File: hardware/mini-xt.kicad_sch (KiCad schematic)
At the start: 0 parts

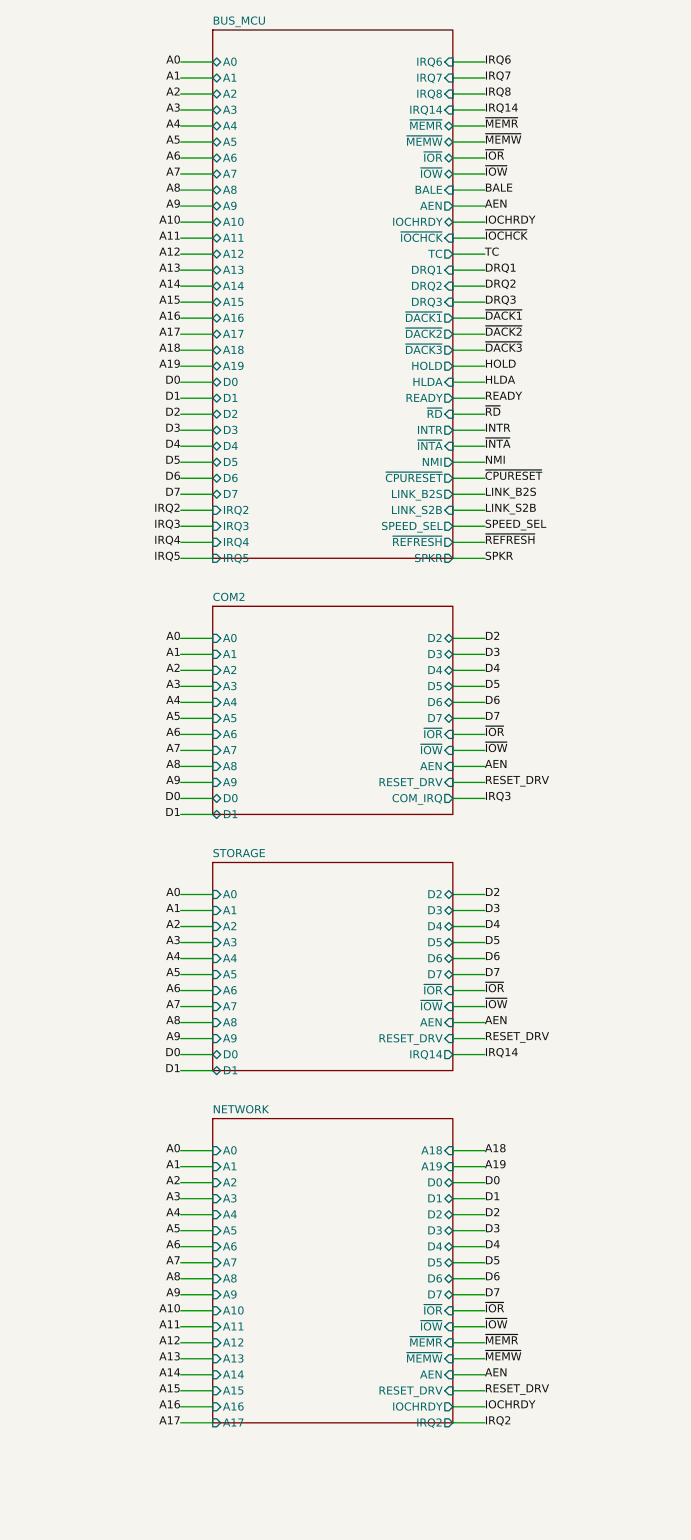
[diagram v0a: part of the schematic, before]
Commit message: bus_mcu: direct 3.3V bus GPIOs (LVC245s+DIR logic deleted); EXT IRQ/DRQ scan
Deleted all six 74LVC245A (data/strobes/address+BALE/AEN-TC) and their DIR
logic; each MCU GPIO now sits on its 3.3V bus net 1:1 (RP2350B is 5V-tolerant
and tri-states natively). Freed GPIO43 (ex-DATADIR) -> EXP_DDIR. Moved the
'165 IRQ collector, the counter '244 output-enable stage and its inverter to
+3V3 (74HC values). Added a 2x 74HC165 EXT scan chain (U19/U20) for the
expansion-port EXT_IRQ2-8/EXT_DRQ1-3 lines. Kept U14-U16 '244s (deviation
from the brief): they are the '163 counter's only tri-state, not level
shifters -- deleting them would fight cpu_core's '573 latches on A0-A19.

Co-Authored-By: Claude Fable 5 <noreply@anthropic.com>
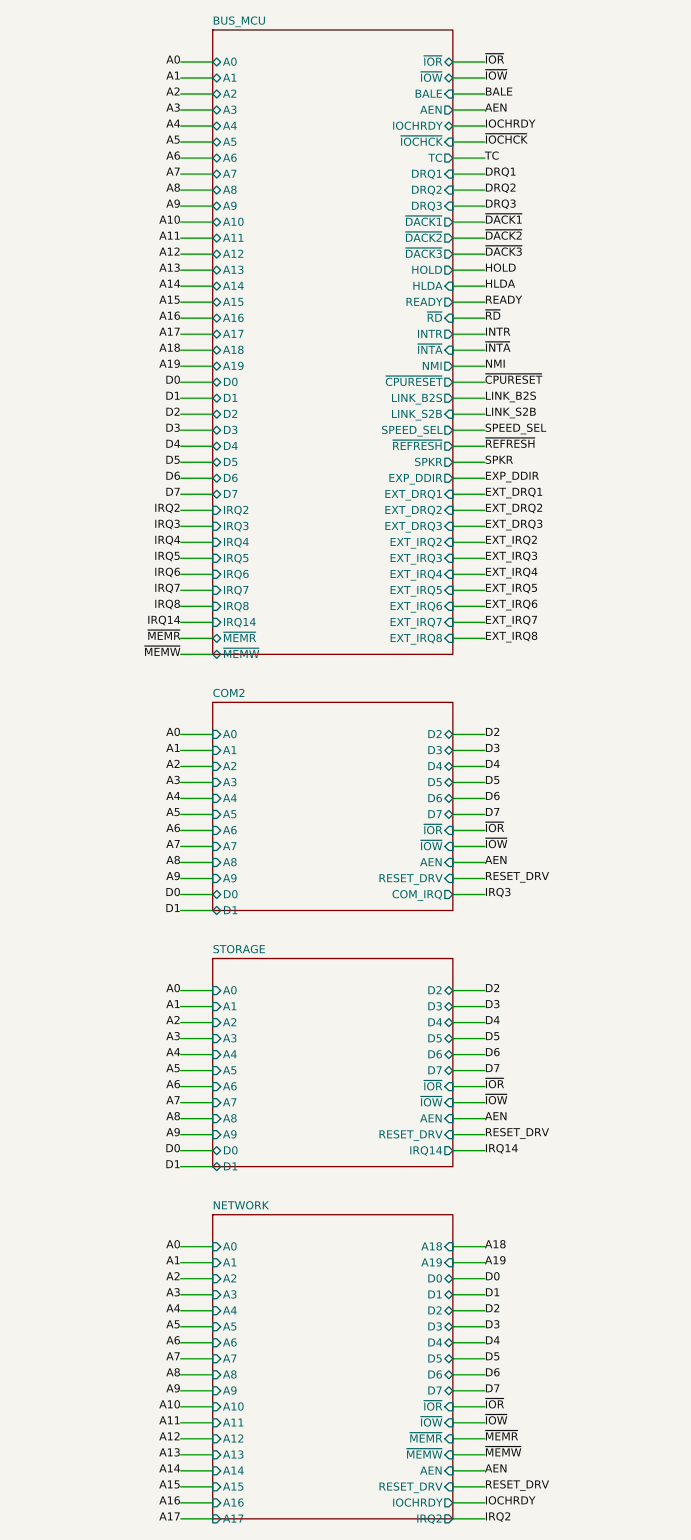
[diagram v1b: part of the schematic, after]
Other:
- sheet BUS_MCU ports: added EXP_DDIR, EXT_DRQ1, EXT_DRQ2, EXT_DRQ3, EXT_IRQ2, EXT_IRQ3, EXT_IRQ4, EXT_IRQ5, EXT_IRQ6, EXT_IRQ7, EXT_IRQ8; removed none

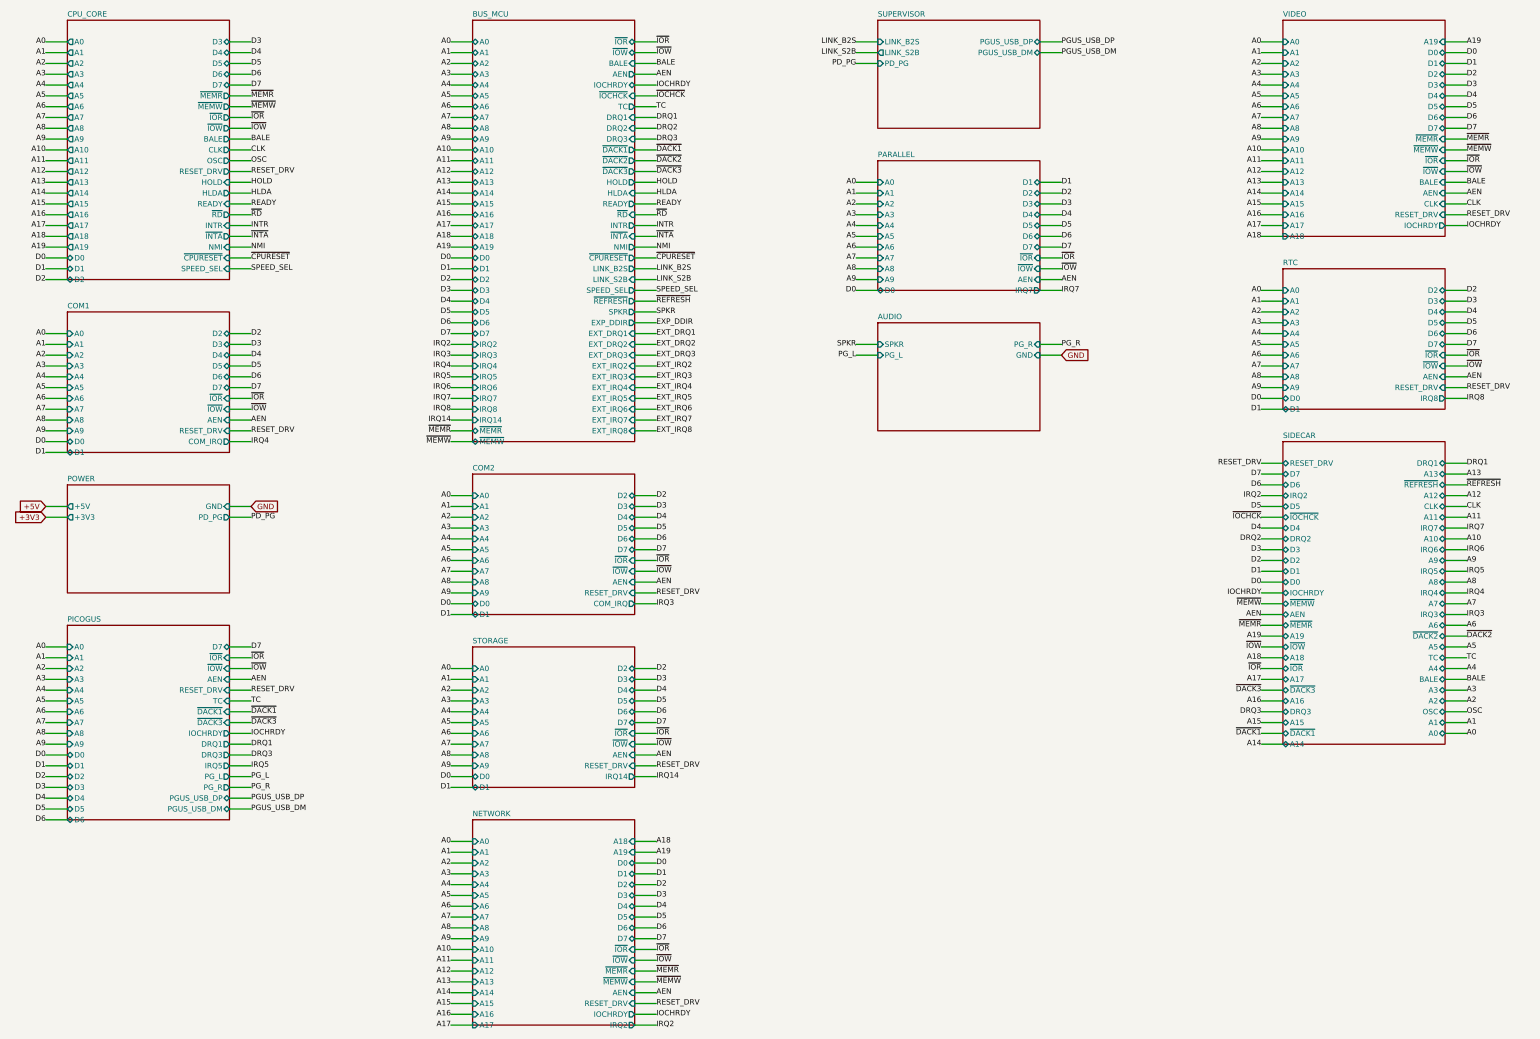
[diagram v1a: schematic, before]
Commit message: RTC: DS12C887 sheet deleted; I2C RTC + coin cell on Supervisor
The Bus MCU now emulates ports 0x70/71 in firmware; real timekeeping moves
to a PCF8563 I2C RTC + CR2032 backup cell on the Supervisor (off-bus, synced
over the existing UART link at boot). rtc.py/rtc.kicad_sch are deleted and
"rtc" is dropped from build.py's SHEETS list (root + 12 sheets).

supervisor.py: PCF8563 (U5) on GPIO2/GPIO3 (RP2040's default I2C1 pins,
picked from the spare-GPIO pool), 4.7k pull-ups to +3V3, a two-Schottky
diode-OR (+3V3 / CR2032) onto VDD_RTC with 100nF decoupling, and the
32.768kHz crystal per the PCF8563 datasheet's single-external-cap topology
(one integrated cap on OSCO, one external trim cap on OSCI -- reused the
already-sourced 22pF rather than add a new SKU). ~{INT}/CLKOUT are NC.
RTC_SDA/RTC_SCL are supervisor-internal nets, not in PINS.

parts.py gains a 32.768kHz crystal entry (C32346, JLC's deepest-stock part,
CL=12.5pF matching the datasheet's own ceiling). bus_mcu.py gets a one-line
note on the 0x70/71 emulation and a flag that IRQ8 (previously driven by
rtc.py) is now genuinely undriven -- left as a follow-up, out of scope here.
Decisions logged in questions-supervisor.md #8.

Co-Authored-By: Claude Fable 5 <noreply@anthropic.com>
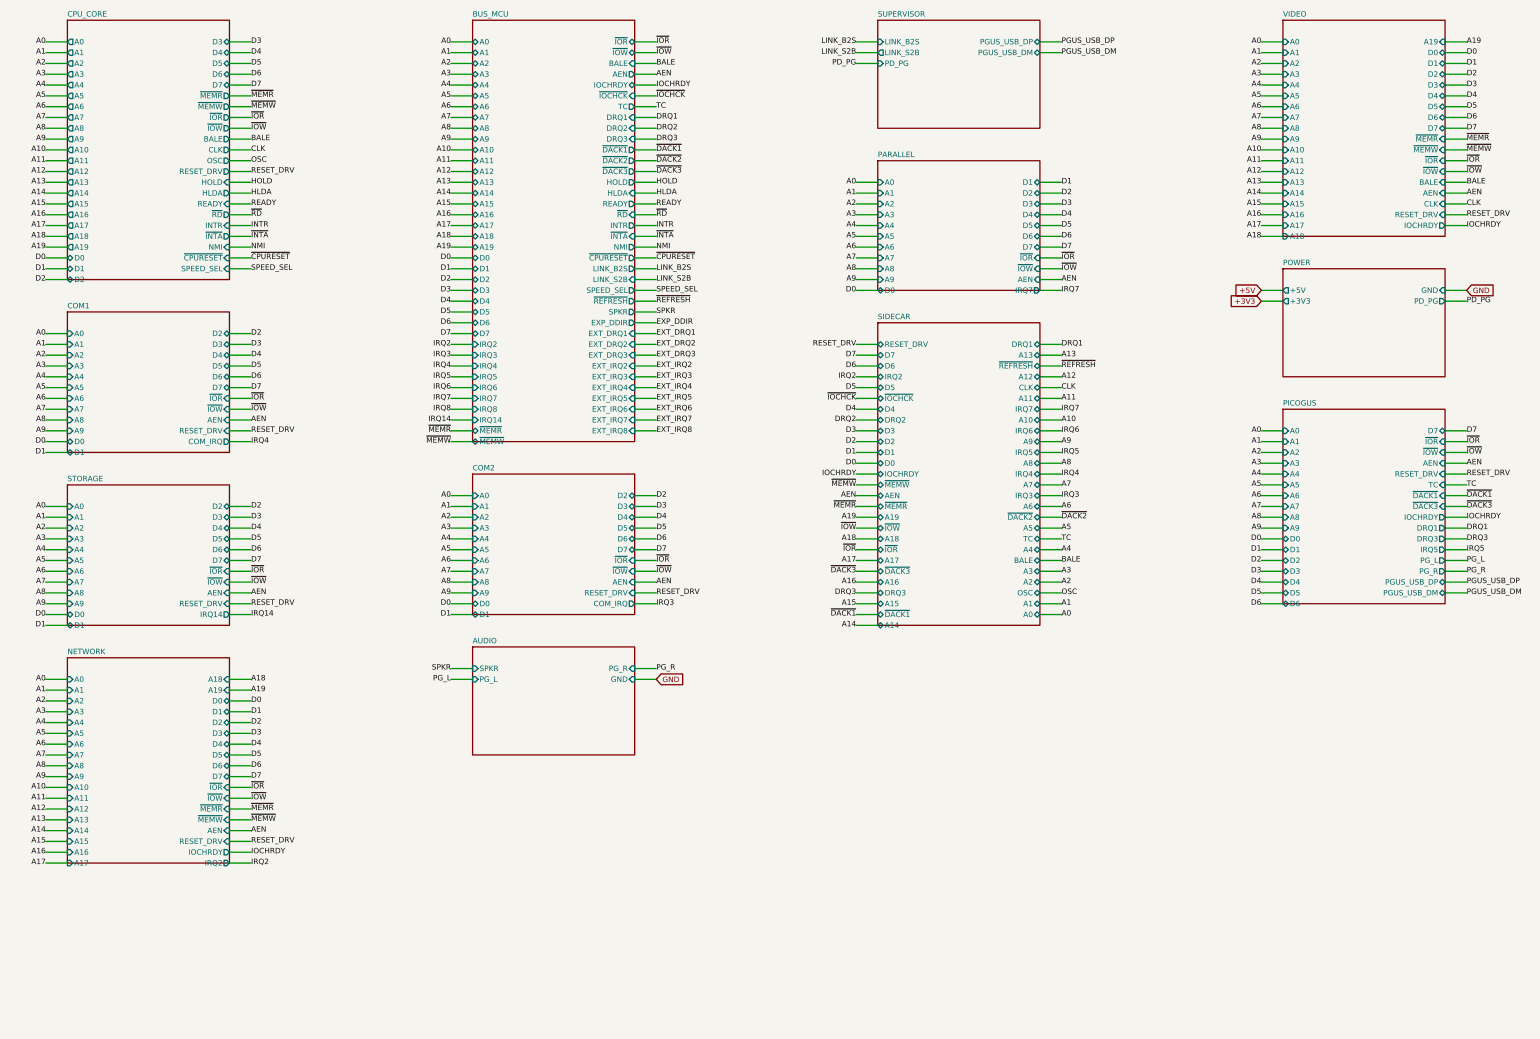
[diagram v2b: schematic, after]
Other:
- removed sheet RTC

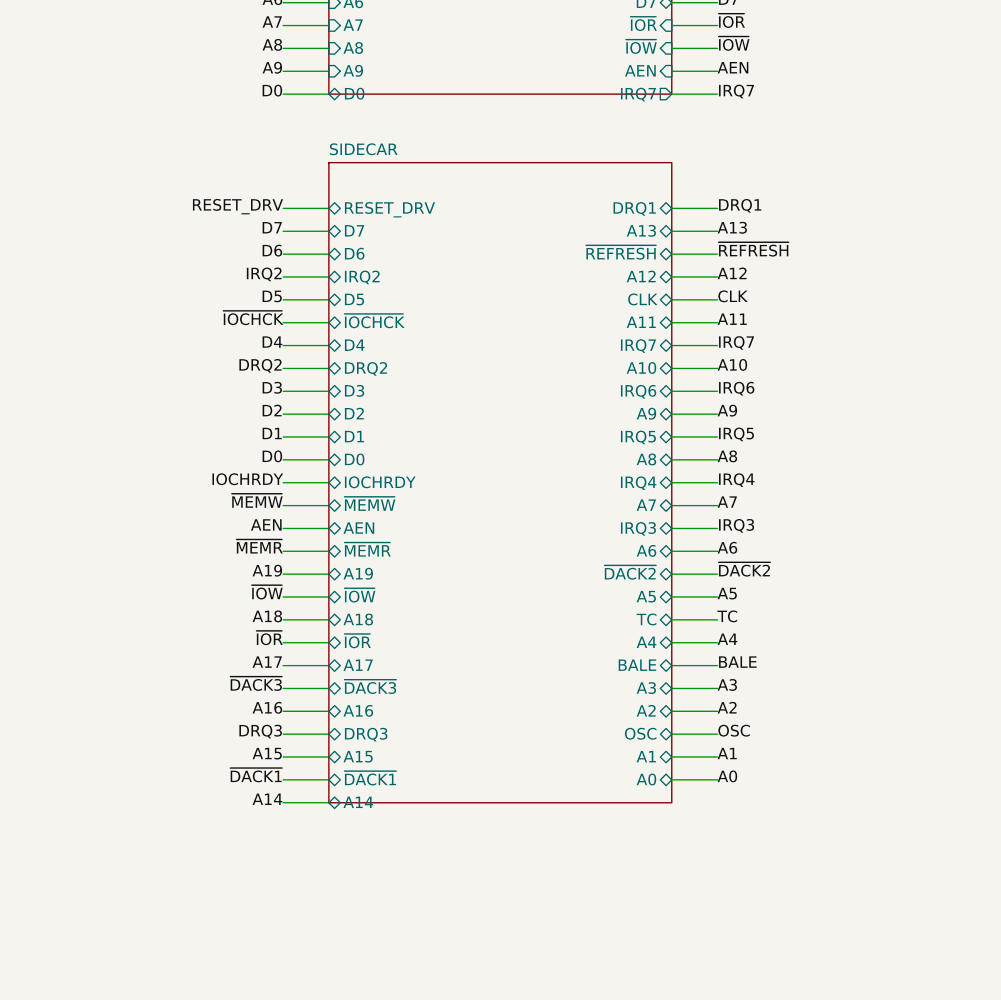
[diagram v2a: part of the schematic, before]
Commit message: sidecar: isolation/buffer bank -- 5V-compatible ISA expansion port
Rewrite the sidecar from a passive 60-pin pass-through into the 3.3V board's
only real-ISA attachment point: an LVC buffer bank (5V-tolerant inputs,
3.3V-TTL outputs) between the internal bus and an external ISA header whose
bus-side nets are port-local (X_*, via isa_conn remap).

- Outbound: 3x 74LVC245A (A0-19 + BALE/AEN/CLK/OSC, DIR strapped outbound) +
  2x 74LVC244A (MEMR/MEMW/IOR/IOW, RESET_DRV, TC, DACK1-3, REFRESH).
- Data: 1x 74LVC245A, DIR = EXP_DDIR, R1 pulls it outbound-safe at power-on
  (DIR=H => A->B; truth table in comment). ~OE tied enabled.
- Inbound: X_IRQ2-7/X_DRQ1-3 -> EXT_* via 2x 74LVC244A, 100k pull-downs on
  every X_ input (unplugged reads all-zeros).
- IOCHRDY/~{IOCHCK}: 74LVC2G07 open-drain (2G06 body + value override) drives
  the internal nets, 10k pull-ups on the X_ side (wired-AND, no contention).
- PINS: filtered copy of isa_conn.ISA_PINS (IRQ/DRQ dropped -> EXT_*), plus
  PRIV_EXP (EXP_DDIR in, EXT_* out); IOCHRDY/~{IOCHCK} kept.

Also refreshes stale build outputs from earlier 3v3 tasks that had edited
sources without rebuilding (network/picogus sheets, card_video net renames),
so committed outputs match current sources. validate_sheet sidecar: zero
structural; build.py exit 0.

Co-Authored-By: Claude Fable 5 <noreply@anthropic.com>
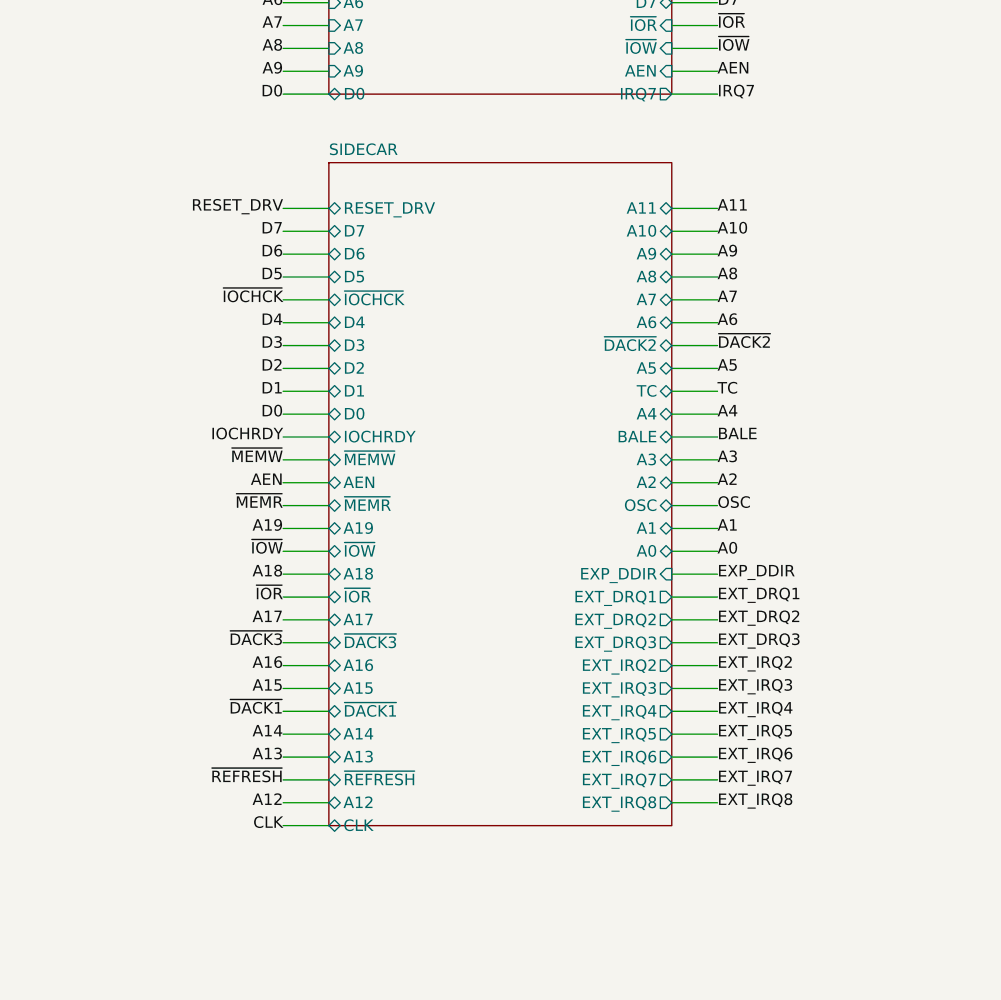
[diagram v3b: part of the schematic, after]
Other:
- sheet SIDECAR ports: added EXP_DDIR, EXT_DRQ1, EXT_DRQ2, EXT_DRQ3, EXT_IRQ2, EXT_IRQ3, EXT_IRQ4, EXT_IRQ5, EXT_IRQ6, EXT_IRQ7, EXT_IRQ8; removed DRQ1, DRQ2, DRQ3, IRQ2, IRQ3, IRQ4, IRQ5, IRQ6, IRQ7
